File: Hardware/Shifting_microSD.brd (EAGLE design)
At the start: 20.4 x 24.6 mm, 21 parts, among them J1 USD_CONNECTOR, Q1 200mA/50V, Q2 200mA/50V, Q3 200mA/50V, Q4 200mA/50V, U2 3.3V

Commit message: Initial design finished
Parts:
- removed Q1, Q2, Q3, Q4: 200mA/50V, SparkFun-DiscreteSemi:SOT23-3
- removed R10, R11, R4, R5, R6, R7, R8, R9: 10K, SparkFun-Resistors:0603-RES
- added C3, C4: 0.1uF, SparkFun-Capacitors:0603-CAP
- added FID1, FID2, FID3, FID4: FIDUCIAL1X2, SparkFun-Aesthetics:FIDUCIAL-1X2
- added LOGO1: SFE_LOGO_FLAME.3_INCH, SparkFun-Aesthetics:SFE_LOGO_FLAME_.3
- added LOGO2: OSHW-LOGOS, SparkFun-Aesthetics:OSHW-LOGO-S
- added U1: (no value), SparkFun-DigitalIC:SO14
- moved JP1 18.9 mm to (16.8, 1.52), turned to 180 degrees
- moved C2 13.9 mm to (5.60, 14.9)
- moved U2 13.9 mm to (3.31, 14.7)
- moved C1 13.0 mm to (0.95, 12.5), turned to 270 degrees
- moved R3 8.67 mm to (3.71, 7.37), turned to 270 degrees
- moved R1 2.96 mm to (7.14, 14.5)
- moved J1 1.49 mm to (16.1, 6.79)
- moved R2 1.01 mm to (14.8, 14.5)
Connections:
- removed net !CS: J1.CS, Q4.2, R10.1
- removed net N$2: JP1.5, Q3.3, R9.1
- removed net N$5: JP1.4, Q2.3, R7.1
- removed net N$7: JP1.3, Q1.3, R5.1
- removed net SCK: J1.SCLK, Q2.2, R6.1
- removed net VCC: C1.1, JP1.7, R11.2, R5.2, R7.2, R9.2, U2.1, U2.3
- new net !CS_3V3: J1.CS, U1.2
- new net 3.3V: C4.1, U1.1, U1.8
- new net DI_3V3: J1.DI, U1.3
- new net DO_3V3: J1.DO, U1.5
- new net N$3: JP1.4, U1.11
- new net SCK_3V3: J1.SCLK, U1.4
- new net VDD_IO: C1.1, C3.1, JP1.7, R3.2, U1.14, U2.1, U2.3
- net 3V3: no longer Q1.1, Q2.1, Q3.1, Q4.1, R10.2, R3.2, R4.2, R6.2, R8.2
- net DI: now also JP1.5, U1.12; no longer J1.DI, Q3.2, R8.1
- net DO: now also JP1.3, U1.10; no longer J1.DO, Q1.2, R4.1
- net GND: now also C3.2, C4.2, U1.7
- net N$1: now also U1.13; no longer Q4.3, R11.1
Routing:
- net 3V3: track 48.5 -> 16.1 mm, vias 6 -> 1
- net N$1: track 30.2 -> 6.81 mm
- net VDD_IO: track 0.00 -> 22.6 mm
- net VCC: track 21.5 -> 0.00 mm
- net N$2: track 21.4 -> 0.00 mm, vias 2 -> 0
- net SCK: track 17.6 -> 0.00 mm, vias 2 -> 0
- net N$7: track 15.1 -> 0.00 mm, vias 2 -> 0
- net N$5: track 14.7 -> 0.00 mm, vias 2 -> 0
- net 3.3V: track 0.00 -> 14.2 mm, vias 0 -> 2
- net CD: track 21.6 -> 8.91 mm
- net !CS: track 7.18 -> 0.00 mm, vias 1 -> 0
- net DO_3V3: track 0.00 -> 6.00 mm, vias 0 -> 1
- net N$3: track 0.00 -> 5.76 mm
- net SCK_3V3: track 0.00 -> 5.61 mm, vias 0 -> 1
- net DI_3V3: track 0.00 -> 5.50 mm, vias 0 -> 1
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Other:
- board size 20.4 x 24.6 mm -> 18.3 x 25.1 mm

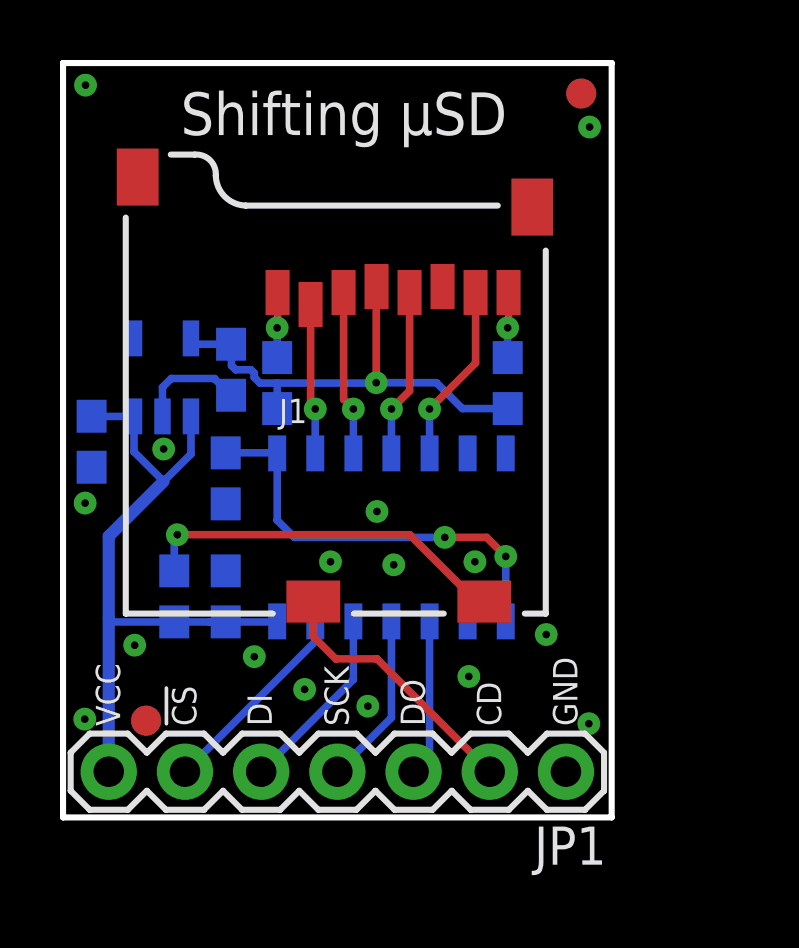
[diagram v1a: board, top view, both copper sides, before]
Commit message: Added CS pull-up
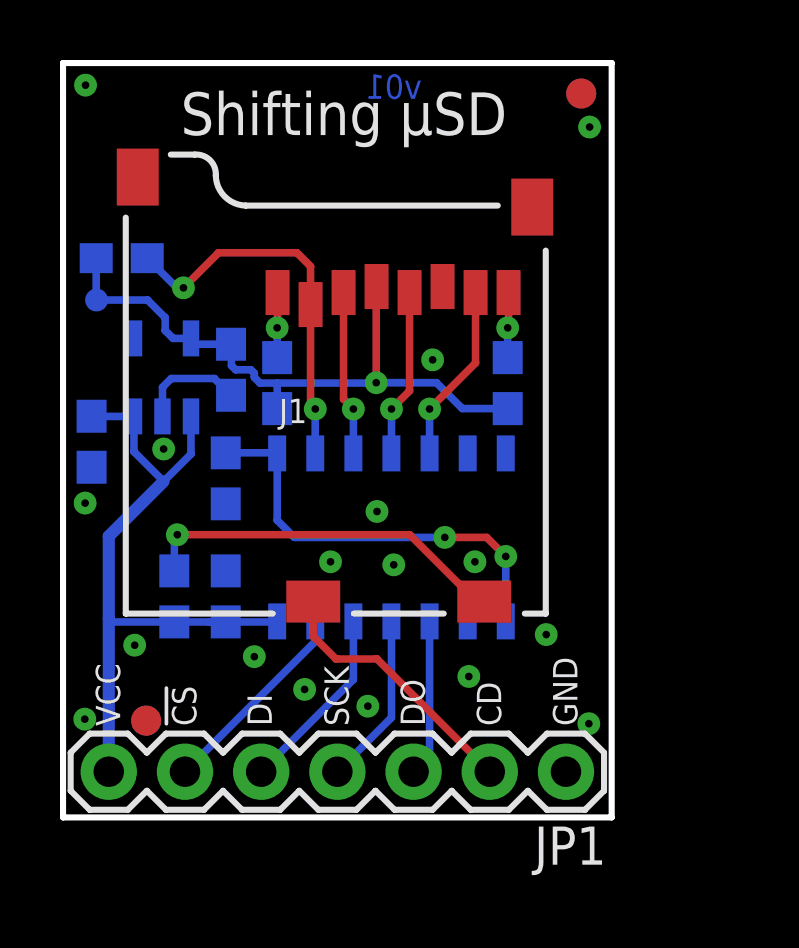
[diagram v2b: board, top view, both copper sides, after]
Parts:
- added R4: 100k, SparkFun-Resistors:0603-RES
- added TP1: TEST-POINT3, SparkFun-Passives:PAD.03X.03
- U1: value (none) -> TXB0104
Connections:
- net !CS_3V3: now also R4.1
- net 3V3: now also R4.2, TP1.P$1
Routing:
- net !CS_3V3: track 5.12 -> 12.9 mm, vias 1 -> 2
- net 3V3: track 16.1 -> 21.4 mm
- net GND: vias 16 -> 17
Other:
- board text added: ">VERSION"
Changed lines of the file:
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@@
 <layer number="113" name="IDFDebug" color="4" fill="1" visible="yes" active="yes"/>
 <layer number="114" name="Badge_Outline" color="11" fill="1" visible="no" active="no"/>
+<layer number="115" name="ReferenceISLANDS" color="7" fill="1" visible="yes" active="yes"/>
 <layer number="116" name="Patch_BOT" color="9" fill="4" visible="yes" active="yes"/>
 <layer number="118" name="Rect_Pads" color="7" fill="1" visible="yes" active="yes"/>
@@
 <dimension x1="0" y1="0" x2="0" y2="25.146" x3="-1.6256" y3="12.573" textsize="1.778" textratio="15" layer="47" unit="inch"/>
 <dimension x1="0" y1="25.146" x2="18.288" y2="25.146" x3="9.144" y3="28.1178" textsize="1.778" textratio="15" layer="47" unit="inch"/>
+<text x="11.0236" y="24.765" size="0.8128" layer="16" font="vector" ratio="15" rot="MR0" align="top-center">&gt;VERSION</text>
 </plain>
 <attributes>
+<attribute name="VERSION" value="v01"/>
 </attributes>
 <variantdefs>
@@
 <element name="LOGO1" library="SparkFun-Aesthetics" package="SFE_LOGO_FLAME_.3" value="SFE_LOGO_FLAME.3_INCH" x="9.1059" y="15.3035" rot="MR0"/>
 <element name="LOGO2" library="SparkFun-Aesthetics" package="OSHW-LOGO-S" value="OSHW-LOGOS" x="12.7889" y="20.447" rot="MR0"/>
-<element name="U1" library="SparkFun-DigitalIC" package="SO14" value="" x="10.9474" y="9.3345" rot="MR180">
+<element name="U1" library="SparkFun-DigitalIC" package="SO14" value="TXB0104" x="10.9474" y="9.3345" rot="MR180">
 <attribute name="PROD_ID" value="IC-11329" x="10.9474" y="9.3345" size="1.778" layer="28" rot="MR180" display="off"/>
 </element>
@@
 <element name="FID3" library="SparkFun-Aesthetics" package="FIDUCIAL-1X2" value="FIDUCIAL1X2" x="17.272" y="24.13"/>
 <element name="FID4" library="SparkFun-Aesthetics" package="FIDUCIAL-1X2" value="FIDUCIAL1X2" x="2.7686" y="3.2258"/>
+<element name="R4" library="SparkFun-Resistors" package="0603-RES" value="100k" x="1.9558" y="18.6436" rot="MR0">
+<attribute name="PROD_ID" value="RES-07828" x="1.9558" y="18.6436" size="1.778" layer="28" rot="MR0" display="off"/>
+</element>
+<element name="TP1" library="SparkFun-Passives" package="PAD.03X.03" value="TEST-POINT3" x="1.1176" y="17.2466" rot="MR0"/>
 </elements>
 <signals>
@@
 <wire x1="6.3754" y1="14.8082" x2="6.2611" y2="14.9225" width="0.254" layer="16"/>
 <wire x1="6.2611" y1="14.9225" x2="5.7531" y2="14.9225" width="0.254" layer="16"/>
+<contactref element="R4" pad="2"/>
+<wire x1="4.2647" y1="15.9686" x2="3.6656" y2="15.9686" width="0.254" layer="16"/>
+<wire x1="3.6656" y1="15.9686" x2="3.4036" y2="16.2306" width="0.254" layer="16"/>
+<wire x1="3.4036" y1="16.2306" x2="3.4036" y2="16.6624" width="0.254" layer="16"/>
+<wire x1="3.4036" y1="16.6624" x2="2.8194" y2="17.2466" width="0.254" layer="16"/>
+<wire x1="2.8194" y1="17.2466" x2="1.1312" y2="17.2466" width="0.254" layer="16"/>
+<contactref element="TP1" pad="P$1"/>
+<wire x1="1.1058" y1="18.6436" x2="1.1058" y2="17.272" width="0.254" layer="16"/>
+<wire x1="1.1312" y1="17.2466" x2="1.1058" y2="17.272" width="0.254" layer="16"/>
+<wire x1="1.1312" y1="17.2466" x2="1.1176" y2="17.2466" width="0.254" layer="16"/>
 </signal>
 <signal name="!CS_3V3">
@@
 <via x="8.4074" y="13.6144" extent="1-16" drill="0.254"/>
 <wire x1="8.4074" y1="13.6144" x2="8.4074" y2="12.1345" width="0.254" layer="16"/>
+<contactref element="R4" pad="1"/>
+<wire x1="2.8058" y1="18.6436" x2="3.7964" y2="17.653" width="0.254" layer="16"/>
+<wire x1="3.7964" y1="17.653" x2="4.0132" y2="17.653" width="0.254" layer="16"/>
+<via x="4.0132" y="17.653" extent="1-16" drill="0.254"/>
+<wire x1="4.0132" y1="17.653" x2="5.1816" y2="18.8214" width="0.254" layer="1"/>
+<wire x1="5.1816" y1="18.8214" x2="7.7978" y2="18.8214" width="0.254" layer="1"/>
+<wire x1="7.7978" y1="18.8214" x2="8.2509" y2="18.3683" width="0.254" layer="1"/>
+<wire x1="8.2509" y1="18.3683" x2="8.2509" y2="17.0945" width="0.254" layer="1"/>
 </signal>
 <signal name="DI_3V3">
@@
 <via x="0.7366" y="10.4775" extent="1-16" drill="0.254"/>
 <via x="3.3528" y="12.2809" extent="1-16" drill="0.254"/>
+<via x="12.319" y="15.2527" extent="1-16" drill="0.254"/>
 </signal>
 <signal name="VDD_IO">
